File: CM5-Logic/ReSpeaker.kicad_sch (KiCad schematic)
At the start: 4 parts, among them J10 63453-116LF, J9 63453-116LF

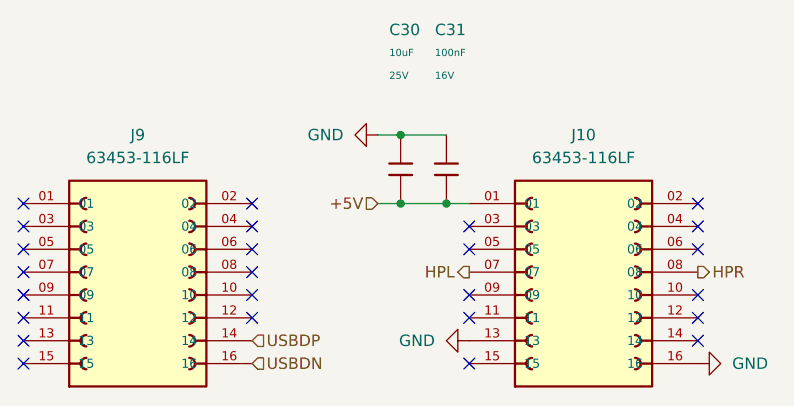
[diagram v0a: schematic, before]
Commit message: adds power connector and works on the ESP32 outputs
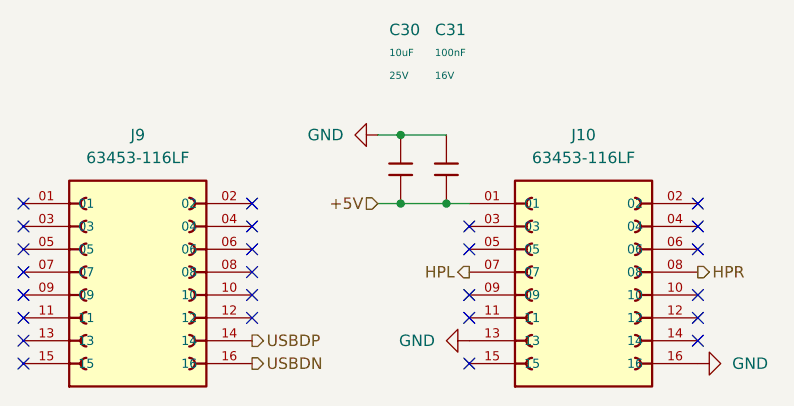
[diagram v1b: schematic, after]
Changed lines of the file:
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@@
 	)
 	(hierarchical_label "USBDP"
-		(shape input)
+		(shape output)
 		(at 130.81 93.98 0)
 		(effects
@@
 	)
 	(hierarchical_label "USBDN"
-		(shape input)
+		(shape output)
 		(at 130.81 96.52 0)
 		(effects

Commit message: fixes a few label issues
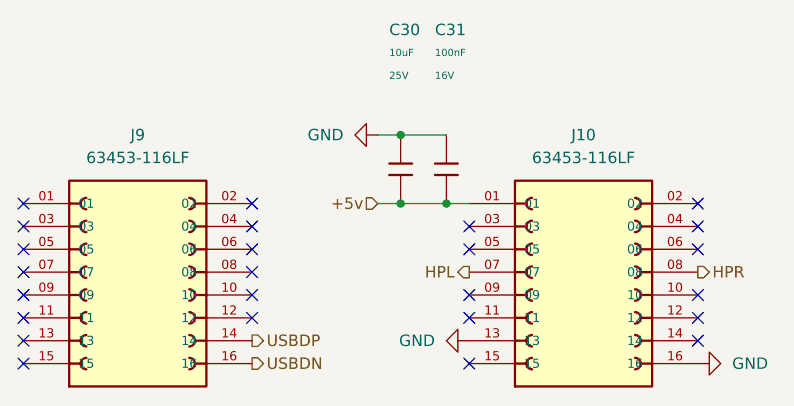
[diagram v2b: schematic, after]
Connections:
- net +5V renamed +5v
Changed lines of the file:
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@@
 		)
 	)
-	(hierarchical_label "+5V"
+	(hierarchical_label "+5v"
 		(shape input)
 		(at 144.78 78.74 180)

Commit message: changes USB port, adds TMC2209 SilentStepStick footprint, redoes PCB Layout
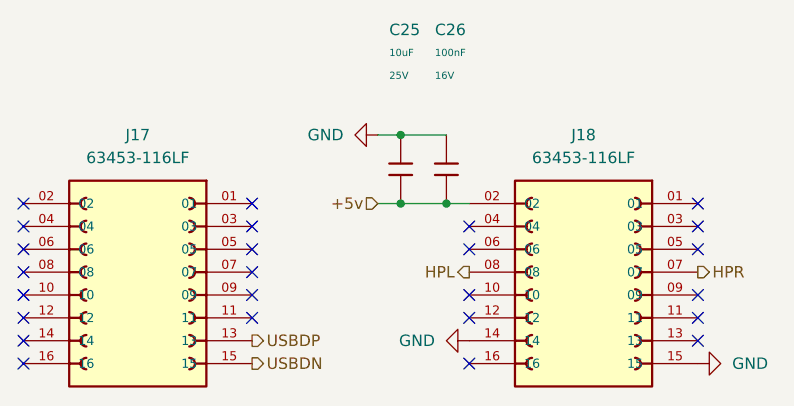
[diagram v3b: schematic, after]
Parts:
- removed J10: 63453-116LF, 63453-116LF:AMPHENOL_63453-116LF, symbol 63453-116LF:63453-116LF
- added J18: 63453-116LF, Custom Components:AMPHENOL_63453-116LF, symbol 63453-116LF:63453-116LF
- J17: renamed from J9; footprint 63453-116LF:AMPHENOL_63453-116LF -> Custom Components:AMPHENOL_63453-116LF
- renumbered C30 to C25, C31 to C26
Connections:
- net +5v: now also J18.02
- net GND: now also J18.14, J18.15
- net HPL: now also J18.08
- net HPR: now also J18.07
- net USBDN: now also J17.15; no longer J17.16
- net USBDP: now also J17.13; no longer J17.14
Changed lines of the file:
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@@
 		(on_board yes)
 		(dnp no)
-		(property "Reference" "#PWR027"
+		(property "Reference" "#PWR067"
 			(at 186.69 96.52 0)
 			(effects
@@
 			(project "CM5IO"
 				(path "/e63e39d7-6ac0-4ffd-8aa3-1841a4541b55/42efa3ee-6442-4474-87b0-fc8afc97b714"
-					(reference "#PWR027")
+					(reference "#PWR067")
 					(unit 1)
 				)
@@
 		(on_board yes)
 		(dnp no)
-		(property "Reference" "C31"
+		(property "Reference" "C26"
 			(at 151.13 59.436 0)
 			(effects
@@
 			(project ""
 				(path "/e63e39d7-6ac0-4ffd-8aa3-1841a4541b55/42efa3ee-6442-4474-87b0-fc8afc97b714"
-					(reference "C31")
+					(reference "C26")
 					(unit 1)
 				)
@@
 	)
 	(symbol
+		(lib_name "63453-116LF_1")
 		(lib_id "63453-116LF:63453-116LF")
 		(at 167.64 88.9 0)
@@
 		(dnp no)
 		(fields_autoplaced yes)
-		(property "Reference" "J10"
+		(property "Reference" "J18"
 			(at 167.64 71.12 0)
 			(effects
@@
 			)
 		)
-		(property "Footprint" "63453-116LF:AMPHENOL_63453-116LF"
+		(property "Footprint" "Custom Components:AMPHENOL_63453-116LF"
 			(at 167.64 88.9 0)
 			(effects
@@
 			(project "CM5IO"
 				(path "/e63e39d7-6ac0-4ffd-8aa3-1841a4541b55/42efa3ee-6442-4474-87b0-fc8afc97b714"
-					(reference "J10")
+					(reference "J18")
 					(unit 1)
 				)
@@
 	)
 	(symbol
+		(lib_name "63453-116LF_1")
 		(lib_id "63453-116LF:63453-116LF")
 		(at 118.11 88.9 0)
@@
 		(dnp no)
 		(fields_autoplaced yes)
-		(property "Reference" "J9"
+		(property "Reference" "J17"
 			(at 118.11 71.12 0)
 			(effects
@@
 			)
 		)
-		(property "Footprint" "63453-116LF:AMPHENOL_63453-116LF"
+		(property "Footprint" "Custom Components:AMPHENOL_63453-116LF"
 			(at 118.11 88.9 0)
 			(effects
@@
 			(project ""
 				(path "/e63e39d7-6ac0-4ffd-8aa3-1841a4541b55/42efa3ee-6442-4474-87b0-fc8afc97b714"
-					(reference "J9")
+					(reference "J17")
 					(unit 1)
 				)
@@
 		(dnp no)
 		(fields_autoplaced yes)
-		(property "Reference" "#PWR09"
+		(property "Reference" "#PWR066"
 			(at 148.59 93.98 0)
 			(effects
@@
 			(project ""
 				(path "/e63e39d7-6ac0-4ffd-8aa3-1841a4541b55/42efa3ee-6442-4474-87b0-fc8afc97b714"
-					(reference "#PWR09")
+					(reference "#PWR066")
 					(unit 1)
 				)
@@
 		(on_board yes)
 		(dnp no)
-		(property "Reference" "C30"
+		(property "Reference" "C25"
 			(at 146.05 59.436 0)
 			(effects
@@
 			(project ""
 				(path "/e63e39d7-6ac0-4ffd-8aa3-1841a4541b55/42efa3ee-6442-4474-87b0-fc8afc97b714"
-					(reference "C30")
+					(reference "C25")
 					(unit 1)
 				)
